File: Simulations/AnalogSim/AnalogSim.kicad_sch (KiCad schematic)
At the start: 2 parts

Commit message: New circuit sim
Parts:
- removed V2: 9, symbol Simulation_SPICE:VDC
- added C1, C2: 47u, symbol Device:C_Polarized_Small_US
- added C10, C9: 100n, symbol Device:C
- added C3, C5, C6, C7, C8: 6n8, symbol Device:C
- added C4: 10u, symbol Device:C_Polarized_Small_US
- added Q4: 2N5088, symbol Simulation_SPICE:NPN
- added Q5, Q6: 2N5087, symbol Simulation_SPICE:PNP
- added R1, R39, R4: 100, symbol Device:R_US
- added R10, R13, R16, R18, R22, R24, R26, R30, R31: 27k, symbol Device:R_US
- added R11: Potentiometer, symbol Simulation_SPICE:Potentiometer
- added R12, R20, R32: 30k, symbol Device:R_US
- added R14, R19, R23, R27, R3: 10k, symbol Device:R_US
- added R15, R17, R21, R25, R40, R41: 1k, symbol Device:R_US
- added R2: 15k, symbol Device:R_US
- added R28: 4k7, symbol Device:R_US
- added R29: 3k3, symbol Device:R_US
- added R33, R8: 470k, symbol Device:R_US
- added R38: 6k8, symbol Device:R_US
- added R5: 2Meg2, symbol Device:R_US
- added R6: 100k, symbol Device:R_US
- added R7: 270k, symbol Device:R_US
- added R9: 51k, symbol Device:R_US
- added SW1: SW_SPDT, Button_Switch_THT:SW_SPDT_Dailywell_Mini_1M, symbol Switch:SW_SPDT
- added U1, U2: LM13700, symbol Amplifier_Operational:LM13700
- added U4: TL074, Package_SO:SOIC-14_3.9x8.7mm_P1.27mm, symbol Amplifier_Operational:TL074
- added V2: VSIN, symbol Simulation_SPICE:VSIN
- added V3: VPULSE, symbol Simulation_SPICE:VPULSE
- added V4: 1.2, symbol Simulation_SPICE:VDC
- V1: value 9 -> 12
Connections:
- net GND: now also C1.2, C2.2, R11.1, R14.2, R19.2, R23.2, R27.2, R28.1, R3.1, R33.2, R38.1, R5.1, SW1.1 (A), U1.6 (V-), U2.6 (V-), U4.11 (V-), V2.2, V3.2, V4.2
- net +9V renamed Vcc
- net Vcc: now also R1.1
- new net: C8.2, U2.5, U2.7
- new net: C5.2, U1.10, U1.12
- new net: R12.1, R13.2, R15.2, U1.13 (-)
- new net: C1.1, R2.1, R3.2, U4.3 (+)
- new net: R28.2, R29.1, R30.2
- new net: C7.2, U1.5, U1.7
- new net: C9.1, R7.1, SW1.2 (B)
- new net: C9.2, R30.1
- new net: R24.1, R25.2, R26.2, U2.4 (-)
- new net: R20.1, R21.2, R22.2, U2.13 (-)
- new net: Q4.3 (E), R38.2, U4.13 (-)
- new net: Q4.1 (C), Q5.1 (C), Q5.2 (B), Q6.2 (B)
- new net: Q4.2 (B), R39.2
- new net: R39.1, U4.14
- new net: R10.1, R9.2, U4.6 (-)
- new net: R11.3, V3.1
- new net: R16.1, R17.2, R18.2, U1.4 (-)
- new net: C6.2, U2.10, U2.12
- new net: C3.1, R6.2, R7.2, SW1.3 (C)
- new net: Q5.3 (E), R40.1
- new net: C10.1, R31.1, R32.2
- new net: C4.2, C5.1, R12.2
- new net: Q6.3 (E), R41.1
- new net A: Q6.1 (C), U1.1, U1.16, U2.1, U2.16
- new net In1: C4.1, R32.1, R9.1, U4.7
- new net InGainIn: C3.2, R8.1, U4.5 (+)
- new net Stg1: C7.1, R13.1, R14.1, R16.2, U1.9
- new net Stg2: C6.1, R18.1, R19.1, R20.2, U1.8
- new net Stg3: C8.1, R22.1, R23.1, R24.2, U2.9
- new net Stg4: R26.1, R27.1, R29.2, R31.2, U2.8
- new net VA: R1.2, R2.2, R4.1, R40.2, R41.2, U1.11 (V+), U2.11 (V+)
- new net VB: R10.2, R15.1, R17.1, R21.1, R25.1, R8.2, U1.14 (+), U1.3 (+), U2.14 (+), U2.3 (+), U4.1, U4.2 (-)
- new net VC: C2.1, R4.2, U4.4 (V+)
- new net Vin: R5.2, R6.1, V2.1
- new net Vlfo: R11.2, U4.12 (+)
- new net Vout: C10.2, R33.1
- no-connect marks 0 -> 8
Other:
- note added: ".options method=gear reltol=0.003 itl4=100 rshunt=1e12"
- note added: ".param ColorOn=0"

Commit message: improved control current range
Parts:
- removed V4: 1.2, symbol Simulation_SPICE:VDC
- added C11: 100n, symbol Device:C
- added R34: 100, symbol Device:R_US
- added R42: 2k2, symbol Device:R_US
- Q4: value 2N5088 -> BC847
- Q5, Q6: value 2N5087 -> BC857
- R20: value 30k -> 27k
- R38: value 6k8 -> 3k3
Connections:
- net GND: no longer R33.2
- net VB: now also R33.2
- net Vout: now also R34.1; no longer C10.2, R33.1
- net at R38.2, U4.13 (-): now also R42.1; no longer Q4.3 (E)
- net at U4.10 (+): now also C10.2, R33.1
- net at U4.8: now also U4.9 (-), C11.1
- new net: C11.2, R34.2
- new net: Q4.3 (E), R42.2
- no-connect marks 8 -> 4
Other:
- moved on the sheet: C10, R27, R31, R33, R38, R41, U4C

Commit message: details and datasheets
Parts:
- removed C2: 47u, symbol Device:C_Polarized_Small_US
- removed R4: 100, symbol Device:R_US
- removed V2: VSIN, symbol Simulation_SPICE:VSIN
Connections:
- net VC is gone; now on net VA: U4.4 (V+)
- net Vin renamed FX_IN
- net Vout renamed FX_OUT

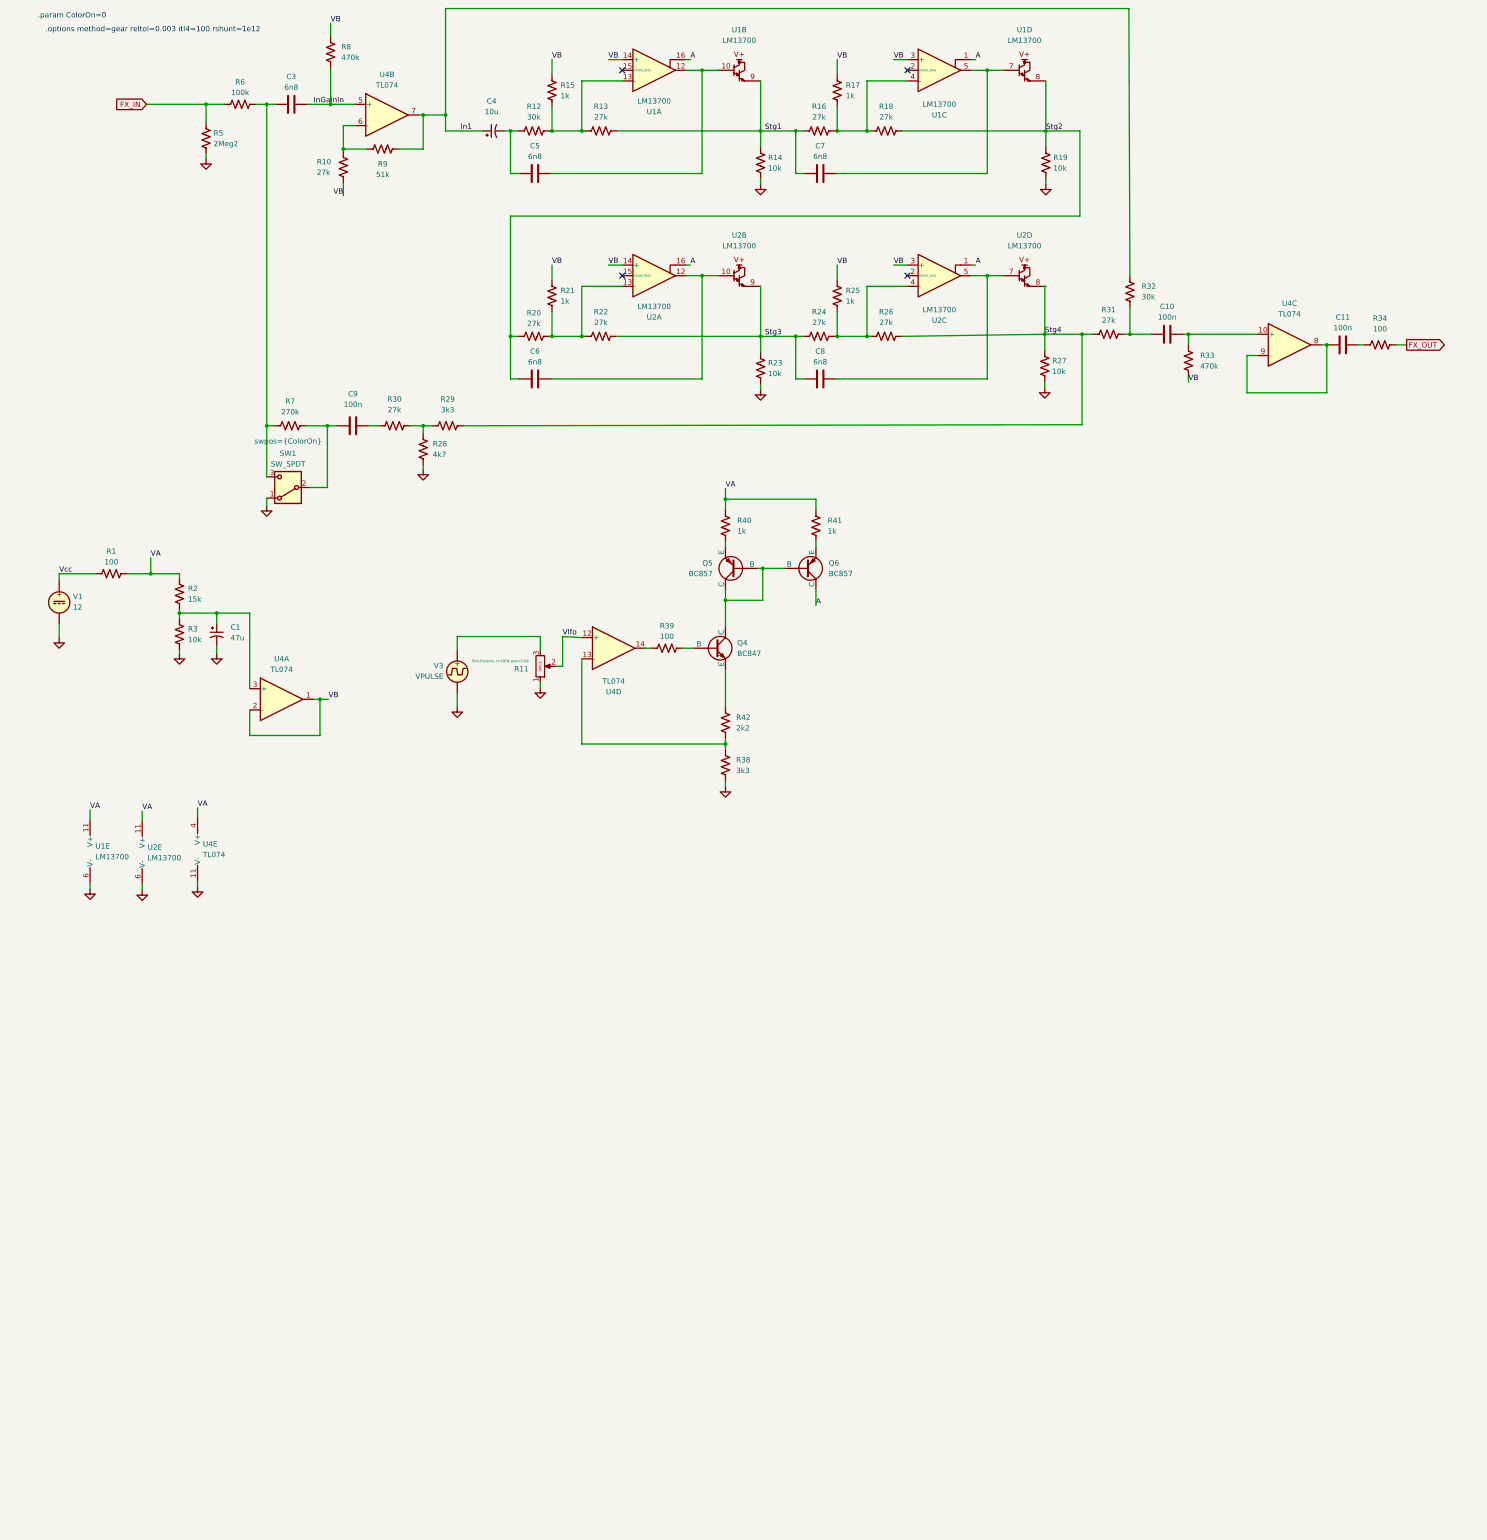
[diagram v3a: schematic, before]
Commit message: Color knob simulation
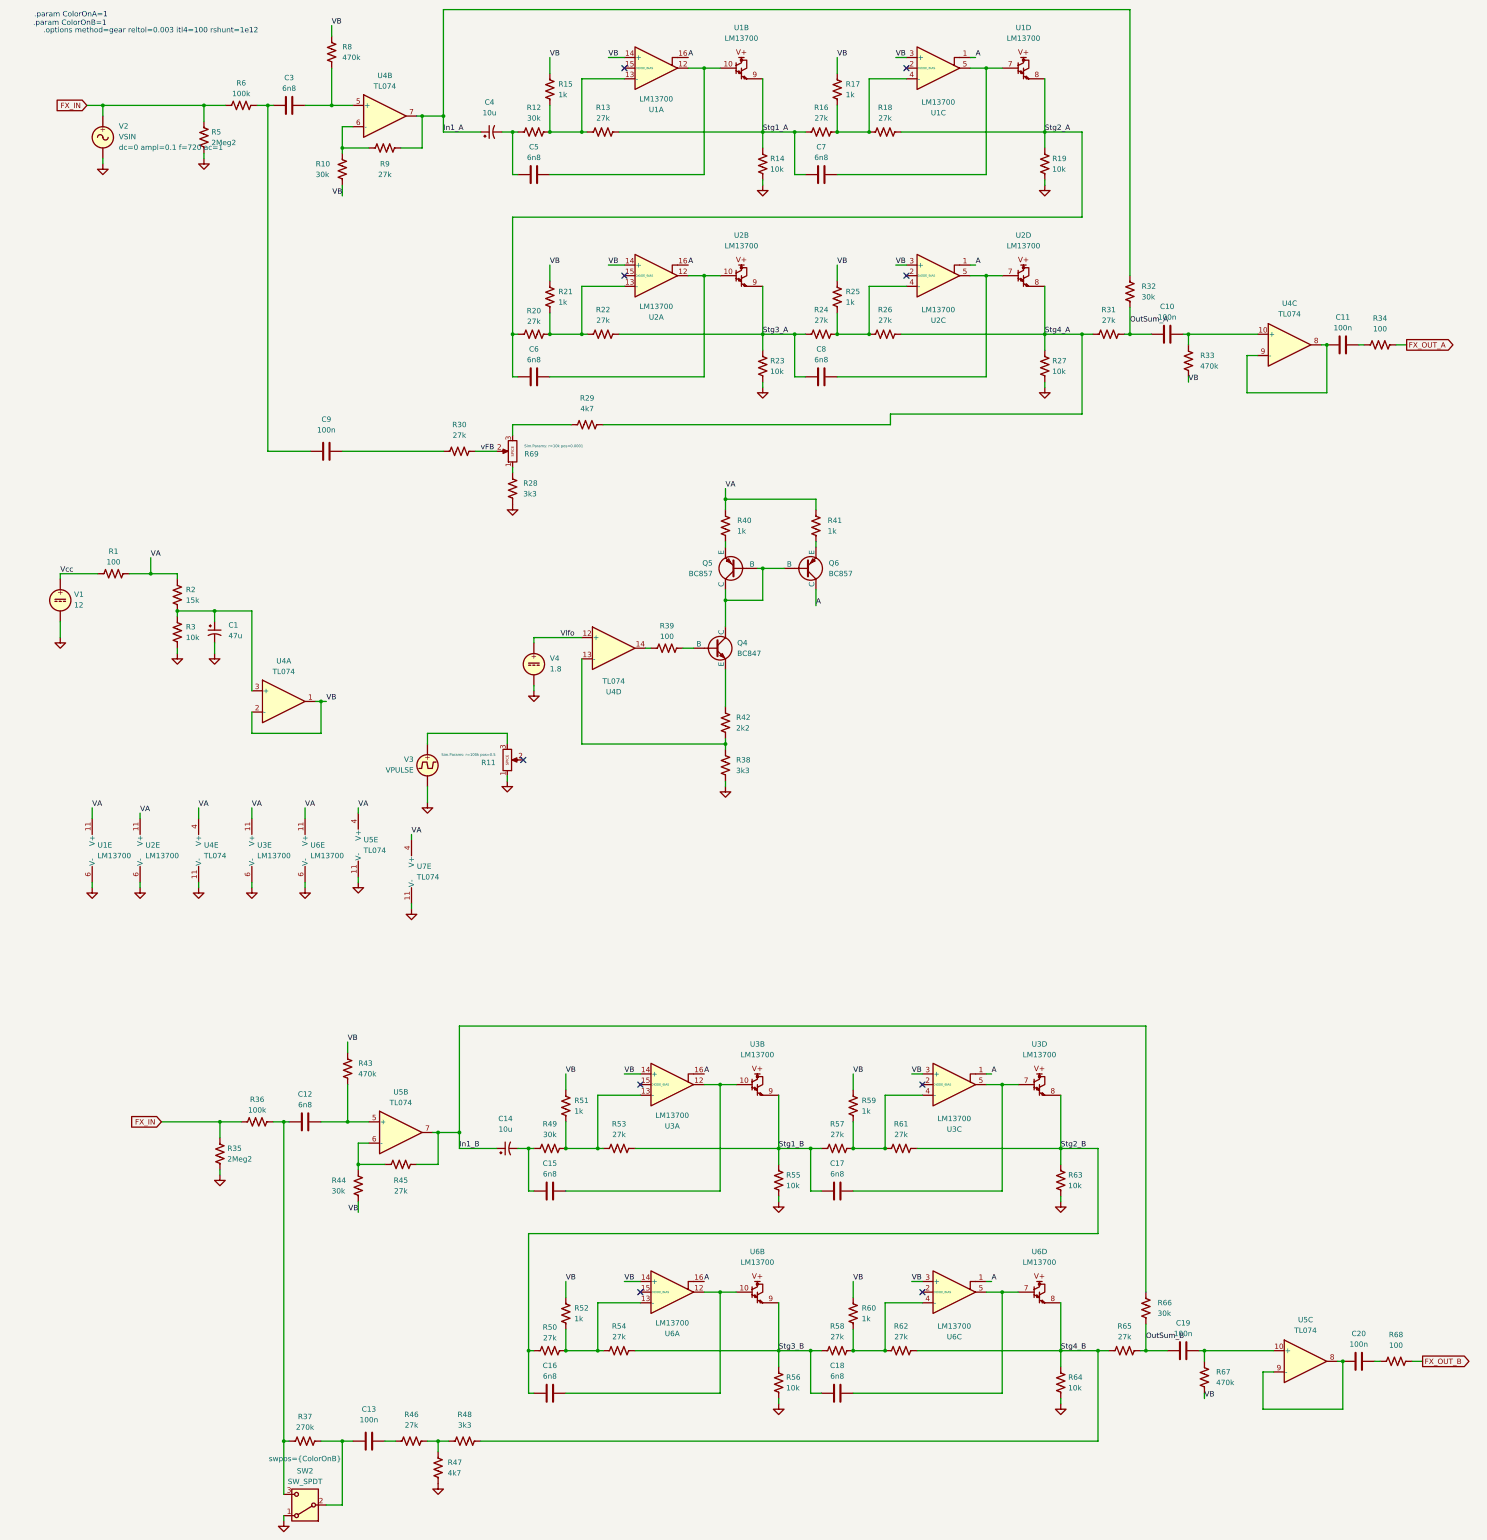
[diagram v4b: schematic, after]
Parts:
- removed R7: 270k, symbol Device:R_US
- removed SW1: SW_SPDT, Button_Switch_THT:SW_SPDT_Dailywell_Mini_1M, symbol Switch:SW_SPDT
- added C12, C15, C16, C17, C18: 6n8, symbol Device:C
- added C13, C19, C20: 100n, symbol Device:C
- added C14: 10u, symbol Device:C_Polarized_Small_US
- added R35: 2Meg2, symbol Device:R_US
- added R36: 100k, symbol Device:R_US
- added R37: 270k, symbol Device:R_US
- added R43, R67: 470k, symbol Device:R_US
- added R44, R49, R66: 30k, symbol Device:R_US
- added R45, R46, R50, R53, R54, R57, R58, R61, R62, R65: 27k, symbol Device:R_US
- added R47: 4k7, symbol Device:R_US
- added R48: 3k3, symbol Device:R_US
- added R51, R52, R59, R60: 1k, symbol Device:R_US
- added R55, R56, R63, R64: 10k, symbol Device:R_US
- added R68: 100, symbol Device:R_US
- added R69: Potentiometer, symbol Simulation_SPICE:Potentiometer
- added SW2: SW_SPDT, Button_Switch_THT:SW_SPDT_Dailywell_Mini_1M, symbol Switch:SW_SPDT
- added U3, U6: LM13700, symbol Amplifier_Operational:LM13700
- added U5, U7: TL074, Package_SO:SOIC-14_3.9x8.7mm_P1.27mm, symbol Amplifier_Operational:TL074
- added V2: VSIN, symbol Simulation_SPICE:VSIN
- added V4: 1.8, symbol Simulation_SPICE:VDC
- R10: value 27k -> 30k
- R28: value 4k7 -> 3k3
- R29: value 3k3 -> 4k7
- R9: value 51k -> 27k
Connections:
- net A: now also U3.1, U3.16, U6.1, U6.16
- net FX_IN: now also R35.2, R36.1, V2.1
- net GND: now also R35.1, R47.1, R55.2, R56.2, R63.2, R64.2, SW2.1 (A), U3.6 (V-), U5.11 (V-), U6.6 (V-), U7.11 (V-), V2.2, V4.2
- net VA: now also U3.11 (V+), U5.4 (V+), U6.11 (V+), U7.4 (V+)
- net VB: now also R43.2, R44.2, R51.1, R52.1, R59.1, R60.1, R67.2, U3.14 (+), U3.3 (+), U6.14 (+), U6.3 (+)
- net Vlfo: now also V4.1; no longer R11.2
- net at C9.1: now also C3.1, R6.2
- net OutSum_A: now reaches C10.1, R31.1, R32.2
- net FX_OUT renamed FX_OUT_A
- net In1 renamed In1_A
- net InGainIn: no longer names the net of C3.2, R8.1, U4.5 (+)
- net Stg1 renamed Stg1_A
- net Stg2 renamed Stg2_A
- net Stg3 renamed Stg3_A
- net Stg4 renamed Stg4_A
- new net: C13.1, R37.1, SW2.2 (B)
- new net: C12.1, R36.2, R37.2, SW2.3 (C)
- new net: C18.2, U6.5, U6.7
- new net: R49.1, R51.2, R53.2, U3.13 (-)
- new net: C14.2, C15.1, R49.2
- new net: R28.2, R69.1
- new net: C19.2, R67.1, U5.10 (+)
- new net: C16.2, U6.10, U6.12
- new net: R50.1, R52.2, R54.2, U6.13 (-)
- new net: R29.1, R69.3
- new net: C12.2, R43.1, U5.5 (+)
- new net: R46.2, R47.2, R48.1
- new net: C20.1, U5.8, U5.9 (-)
- new net: C20.2, R68.2
- new net: C15.2, U3.10, U3.12
- new net: R58.1, R60.2, R62.2, U6.4 (-)
- new net: R57.1, R59.2, R61.2, U3.4 (-)
- new net: C13.2, R46.1
- new net: R44.1, R45.2, U5.6 (-)
- new net: C17.2, U3.5, U3.7
- new net FX_OUT_B: R68.1
- new net In1_B: C14.1, R45.1, R66.1, U5.7
- new net OutSum_B: C19.1, R65.1, R66.2
- new net Stg1_B: C17.1, R53.1, R55.1, R57.2, U3.9
- new net Stg2_B: C16.1, R50.2, R61.1, R63.1, U3.8
- new net Stg3_B: C18.1, R54.1, R56.1, R58.2, U6.9
- new net Stg4_B: R48.2, R62.1, R64.1, R65.2, U6.8
- new net vFB: R30.2, R69.2
- no-connect marks 4 -> 9
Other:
- note added: ".param ColorOnA=1"
- note added: ".param ColorOnB=1"
- note removed: ".param ColorOn=0"
- moved on the sheet: C1, C3, C4, C6, C8, C9, R1, R10, R11, R13, R14, R15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
